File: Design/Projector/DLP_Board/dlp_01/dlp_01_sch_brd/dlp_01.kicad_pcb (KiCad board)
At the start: 6 copper layers, 22.3 x 6 mm, 255 parts, among them J1 Conn_02x40_Odd_Even, J10 Screw_Terminal_01x03, J2 Conn_02x40_Odd_Even, J3 Barrel_Jack_MountingPin, J4 Screw_Terminal_01x03, J5 Screw_Terminal_01x03, J6 Screw_Terminal_01x03, J7 Screw_Terminal_01x03, J8 Screw_Terminal_01x03, J9 Screw_Terminal_01x03, Q1 2N7000, U1 DLPC3437, U2 DLPC3437, U3 ASDMB-24.000MHZ-LC-T, U4 W25Q64JVSSIQ, U5 W25Q64JVSSIQ, U6 DLPA3000, U7 DLP3310AFQM, U8 RPM5.0-3.0, U9 NF_SN74AUP1T17

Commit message: Initial component placement on PCB
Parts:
- C1, C10, C11, C12, C13, C14, C15, C16, C17, C18, C19, C2, C20, C21, C22, C23, C24, C25, C26, C27, C28, C29, C3, C30, C31, C32, C33, C34, C35, C36, C37, C38, C39, C4, C40, C41, C42, C43, C44, C45, C46, C5, C6, C7, C8, C9: footprint Capacitors_SMD:C_0603 -> Capacitors_SMD:C_0402; moved to B.Cu
- C47, C48, C49, C50, C51, D5, J1, J10, J2, J3, J4, J5, Q1, R16, R52, R53, R54, R55, R92, R93, R94, R95, R96, R97, TP1, TP10, TP2, TP3, TP4, TP5, TP6, TP7, TP8, TP9, U3: moved to B.Cu
- FB1, FB2, FB3, FB4: value BLM18KG121TN1D -> BLM15PD800SN1D; footprint Inductors_SMD:L_0603 -> Inductors_SMD:L_0402; moved to B.Cu
- J6, J7, J8, J9: value Screw_Terminal_01x03 -> Conn_01x03_Male; footprint Connectors_Terminal_Blocks:TerminalBlock_bornier-3_P5.08mm -> Pin_Headers:Pin_Header_Straight_1x03_Pitch2.54mm_SMD_Pin1Left; moved to B.Cu
- moved C58 292.9 mm to (132.8, 139.9), turned to 180 degrees
- moved C52 292.0 mm to (130.0, 141.5), turned to 90 degrees
- moved R60 291.1 mm to (125.0, 144.5), turned to 180 degrees
- moved C55 289.4 mm to (127.8, 141.5), turned to 90 degrees
- moved D1 289.3 mm to (132.4, 137.9), turned to 180 degrees
- moved C68 288.4 mm to (125.0, 142.9), turned to 180 degrees
- moved R54 288.4 mm to (114.7, 142.3), turned to 270 degrees
- moved C48 287.8 mm to (116.7, 142.3), turned to 270 degrees
- moved C50 287.1 mm to (118.9, 142.3), turned to 270 degrees
- moved C74 285.8 mm to (125.8, 140.7), turned to 90 degrees
- moved C71 284.7 mm to (129.2, 131.9), turned to 180 degrees
- moved L3 284.0 mm to (132.6, 134.3), turned to 180 degrees
- moved L1 283.2 mm to (123.6, 140.7), turned to 270 degrees
- moved C66 281.6 mm to (121.0, 141.5), turned to 90 degrees
- moved C59 281.3 mm to (129.2, 129.7), turned to 180 degrees
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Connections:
- C12 pad 1: +1V1 -> +1V8
- C13 pad 1: +1V1 -> +1V8
- C15 pad 1: +1V1 -> +1V8
- C16 pad 1: +1V1 -> +1V8
- C18 pad 1: +1V1 -> +1V8
- C19 pad 1: +1V1 -> +1V8
- C21 pad 1: +1V1 -> +1V8
- C22 pad 1: +1V1 -> +1V8
- C24 pad 1: +1V1 -> +1V8
- C25 pad 1: +1V1 -> +1V8
- C26 pad 1: +1V1 -> +1V8
- C27 pad 1: +1V1 -> +1V8
- C29 pad 1: +1V1 -> +1V8
- C3 pad 1: +1V1 -> +1V8
- C30 pad 1: +1V1 -> +1V8
- C34 pad 1: +1V1 -> +1V8
- C35 pad 1: +1V1 -> +1V8
- C38 pad 1: +1V1 -> +1V8
- C39 pad 1: +1V1 -> +1V8
- C4 pad 1: +1V1 -> +1V8
- C41 pad 1: +1V1 -> +1V8
- C42 pad 1: +1V1 -> +1V8
- C8 pad 1: +1V1 -> +1V8
- C9 pad 1: +1V1 -> +1V8
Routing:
- net /dlp_controller/DMD_LS_RDATA: track 0.57 -> 23.3 mm
- net /dlp_controller/DMD_DEN_ARSTZ: track 0.57 -> 16.5 mm
- net /dlp_controller/sDMD_HS_WDATAG_P: track 0.57 -> 15.7 mm
- net /dlp_controller/sDMD_HS_CLK_P: track 0.57 -> 15.6 mm, vias 2 -> 3
- net /dlp_controller/sDMD_HS_WDATAG_N: track 0.57 -> 15.2 mm
- net /dlp_controller/mDMD_HS_WDATAD_N: track 0.57 -> 15.0 mm
- net /dlp_controller/mDMD_HS_WDATAD_P: track 0.57 -> 14.8 mm
- net /dlp_controller/sDMD_HS_WDATAA_N: track 0.57 -> 14.7 mm
- net /dlp_controller/mDMD_HS_WDATAC_N: track 0.57 -> 14.6 mm
- net /dlp_controller/sDMD_HS_WDATAE_N: track 0.57 -> 14.5 mm
- net /dlp_controller/mDMD_HS_WDATAH_N: track 0.57 -> 14.1 mm
- net /dlp_controller/sDMD_HS_WDATAF_N: track 0.57 -> 14.0 mm, vias 2 -> 3
- net /dlp_controller/mDMD_HS_CLK_N: track 0.57 -> 13.7 mm, vias 2 -> 3
- net /dlp_controller/mDMD_HS_WDATAC_P: track 0.57 -> 13.6 mm
- net /dlp_controller/mDMD_HS_WDATAB_N: track 0.59 -> 13.3 mm
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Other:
- board size 22.3 x 6 mm -> 102 x 98 mm
- net class Default: trace_width 0.1524 -> 0.1
- rule trace_min: 0.1524 -> 0.1

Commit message: Schematic and PCB complete ready for review
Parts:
- removed J10: Screw_Terminal_01x03, Connectors_Terminal_Blocks:TerminalBlock_bornier-3_P5.08mm
- removed R100, R101, R102, R103, R104, R105, R75, R76, R84, R85, R86, R87, R88, R90: 22R, Resistors_SMD:R_0603
- removed R79, R83: NF, Resistors_SMD:R_0603
- removed RN1, RN2, RN3: R_Pack08, Resistors_SMD:R_Array_Convex_8x0602
- removed RN4, RN5, RN6: 22R, Resistors_SMD:R_Array_Convex_8x0602
- added H1: 3mm, Mounting_Holes:MountingHole_3mm_Pad_Via, F.Cu at (99.6, 56.7)
- added H2: 3mm, Mounting_Holes:MountingHole_3mm_Pad_Via, F.Cu at (99.6, 147.0)
- added H3: 3mm, Mounting_Holes:MountingHole_3mm_Pad_Via, F.Cu at (195.5, 56.7)
- added H4: 3mm, Mounting_Holes:MountingHole_3mm_Pad_Via, F.Cu at (195.5, 147.0)
- added H5: 3mm, Mounting_Holes:MountingHole_3mm_Pad_Via, F.Cu at (99.6, 113.7)
- added H6: 3mm, Mounting_Holes:MountingHole_3mm_Pad_Via, F.Cu at (195.6, 113.6)
- C49, C51, C81, R55, R57, R97, TP2, TP3, TP4, TP5, TP6, TP7, TP8, TP9: moved to F.Cu
- C53, C56, C57, C61, C66, R10, R11, R12, R19, R35, R36, R37, R39, R41, R42, R43, R44, R46, R47, R51, R81, R82: moved to B.Cu
- R72, R73, R74: value 22R -> NF
- moved TP8 58.2 mm to (157.5, 93.6)
- moved TP9 56.4 mm to (155.2, 93.6)
- moved TP7 53.1 mm to (157.5, 95.9)
- moved TP6 51.1 mm to (155.2, 95.9)
- moved TP5 49.7 mm to (155.2, 98.2)
- moved TP3 48.8 mm to (157.5, 98.2)
- moved TP4 48.4 mm to (155.2, 100.5)
- moved TP2 46.7 mm to (157.5, 100.5)
- moved R81 45.7 mm to (132.5, 117.4), turned to 90 degrees
- moved R82 42.4 mm to (134.1, 117.4), turned to 270 degrees
- moved R29 34.0 mm to (133.6, 105.2), turned to 90 degrees
- moved R89 33.5 mm to (121.2, 109.8), turned to 180 degrees
- moved R71 32.7 mm to (124.8, 66.5), turned to 270 degrees
- moved R12 31.1 mm to (133.4, 121.4), turned to 0 degrees
- moved R28 31.0 mm to (135.2, 105.2), turned to 270 degrees
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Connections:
- net /application_connectors/3DR_A renamed Net-(R50-Pad1)
- net /application_connectors/3DR_B renamed Net-(R48-Pad1)
- J1 pad 15: Net-(J1-Pad15) -> /application_connectors/ZYNQ_VDDIO_13
- J1 pad 19: /application_connectors/IO_B13_LN13 -> /application_connectors/PDM_CVS_TE_B
- J1 pad 21: /application_connectors/IO_B13_LP15 -> /application_connectors/HSYNC_B
- J1 pad 23: /application_connectors/IO_B13_LN15 -> /application_connectors/VSYNC_B
- J1 pad 27: /application_connectors/IO_B34_LP2 -> /application_connectors/DATEN_B
- J1 pad 49: Net-(J1-Pad49) -> /application_connectors/ZYNQ_VDDIO_34
- J2 pad 33: /application_connectors/IO_B35_LP5 -> /application_connectors/FPGA_RDY
- J2 pad 35: /application_connectors/IO_B35_LN5 -> /application_connectors/ACT_SYNC
- J2 pad 37: /application_connectors/IO_B35_LP7 -> /application_connectors/SUB_FRAME
- J2 pad 39: /application_connectors/IO_B35_LN7 -> /application_connectors/PROJ_ON
- J2 pad 43: /application_connectors/IO_B35_LP9 -> /application_connectors/sHOST_IRQ
- J2 pad 45: /application_connectors/IO_B35_LN9 -> /application_connectors/mHOST_IRQ
- J2 pad 46: /application_connectors/IO_B35_LP12 -> /application_connectors/PCLK_A
- J2 pad 51: Net-(J2-Pad51) -> /application_connectors/ZYNQ_VDDIO_35
- J2 pad 53: /application_connectors/IO_B35_LP13 -> /application_connectors/PCLK_B
- J2 pad 65: /application_connectors/IO_B35_LN17 -> /application_connectors/PDM_CVS_TE_A
- J2 pad 67: /application_connectors/IO_B35_LP19 -> /application_connectors/HSYNC_A
- J2 pad 69: /application_connectors/IO_B35_LN19 -> /application_connectors/VSYNC_A
- J2 pad 73: /application_connectors/IO_B35_LP21 -> /application_connectors/DATEN_A
- J3 pad 3: Net-(J3-Pad3) -> GND
- R68 pad 1: Net-(J1-Pad49) -> /application_connectors/ZYNQ_VDDIO_34
- R68 pad 2: /application_connectors/ZYNQ_VDDIO_34 -> +3V3
- R69 pad 1: Net-(J1-Pad15) -> /application_connectors/ZYNQ_VDDIO_13
- R69 pad 2: /application_connectors/ZYNQ_VDDIO_13 -> +3V3
- R72 pad 1: /application_connectors/IO_B13_LN13 -> /application_connectors/ZYNQ_VDDIO_34
- R72 pad 2: /application_connectors/PDM_CVS_TE_B -> +1V8
- R73 pad 1: /application_connectors/IO_B13_LP15 -> /application_connectors/ZYNQ_VDDIO_13
- R73 pad 2: /application_connectors/HSYNC_B -> +1V8
- R74 pad 1: /application_connectors/IO_B13_LN15 -> /application_connectors/ZYNQ_VDDIO_35
- R74 pad 2: /application_connectors/VSYNC_B -> +1V8
- R78 pad 1: Net-(J2-Pad51) -> /application_connectors/ZYNQ_VDDIO_35
- R78 pad 2: /application_connectors/ZYNQ_VDDIO_35 -> +3V3
- U1 pad K1: /application_connectors/PDAT_B_1 -> /application_connectors/LCD_DATA1
- U1 pad K2: /application_connectors/PDAT_B_0 -> /application_connectors/LCD_DATA0
- U1 pad L1: /application_connectors/PDAT_B_3 -> /application_connectors/LCD_DATA3
- U1 pad L2: /application_connectors/PDAT_B_2 -> /application_connectors/LCD_DATA2
- U1 pad M1: /application_connectors/PDAT_B_5 -> /application_connectors/LCD_DATA5
- U1 pad M2: /application_connectors/PDAT_B_4 -> /application_connectors/LCD_DATA4
- U1 pad N1: /application_connectors/PDAT_B_7 -> /application_connectors/LCD_DATA7
- U1 pad N2: /application_connectors/PDAT_B_6 -> /application_connectors/LCD_DATA6
- U1 pad P10: /application_connectors/PDAT_B_23 -> /application_connectors/IO_B34_LP4
- U1 pad P4: /application_connectors/PDAT_B_11 -> /application_connectors/LCD_DATA11
- U1 pad P5: /application_connectors/PDAT_B_13 -> /application_connectors/LCD_DATA13
- U1 pad P6: /application_connectors/PDAT_B_15 -> /application_connectors/LCD_DATA15
- U1 pad P7: /application_connectors/PDAT_B_17 -> /application_connectors/IO_B34_LP11
- U1 pad P8: /application_connectors/PDAT_B_19 -> /application_connectors/IO_B34_LP8
- U1 pad P9: /application_connectors/PDAT_B_21 -> /application_connectors/IO_B34_LP6
- U1 pad R1: /application_connectors/PDAT_B_8 -> /application_connectors/LCD_DATA8
- U1 pad R2: /application_connectors/PDAT_B_9 -> /application_connectors/LCD_DATA9
- U1 pad R3: /application_connectors/PDAT_B_10 -> /application_connectors/LCD_DATA10
- U1 pad R4: /application_connectors/PDAT_B_12 -> /application_connectors/LCD_DATA12
- U1 pad R5: /application_connectors/PDAT_B_14 -> /application_connectors/LCD_DATA14
- U1 pad R6: /application_connectors/PDAT_B_16 -> /application_connectors/IO_B34_LN11
- U1 pad R7: /application_connectors/PDAT_B_18 -> /application_connectors/IO_B34_LN8
- U1 pad R8: /application_connectors/PDAT_B_20 -> /application_connectors/IO_B34_LN6
- U1 pad R9: /application_connectors/PDAT_B_22 -> /application_connectors/IO_B34_LN4
- U2 pad K1: /dlp_controller/dlp_controller_datainterface/PDAT_A_1 -> /application_connectors/IO_B35_LN23
- U2 pad K2: /dlp_controller/dlp_controller_datainterface/PDAT_A_0 -> /application_connectors/IO_B35_LP23
- U2 pad L1: /application_connectors/PDAT_A_3 -> /application_connectors/IO_B35_LP24
- U2 pad L2: /application_connectors/PDAT_A_2 -> /application_connectors/IO_B35_LN24
- U2 pad M1: /application_connectors/PDAT_A_5 -> /application_connectors/IO_B35_LP22
- U2 pad M2: /application_connectors/PDAT_A_4 -> /application_connectors/IO_B35_LN22
- U2 pad N1: /application_connectors/PDAT_A_7 -> /application_connectors/IO_B35_LP20
- U2 pad N2: /application_connectors/PDAT_A_6 -> /application_connectors/IO_B35_LN20
- U2 pad P10: /application_connectors/PDAT_A_23 -> /application_connectors/IO_B35_LP2
- U2 pad P4: /application_connectors/PDAT_A_11 -> /application_connectors/IO_B35_LP16
- U2 pad P5: /application_connectors/PDAT_A_13 -> /application_connectors/IO_B35_LP14
- U2 pad P6: /application_connectors/PDAT_A_15 -> /application_connectors/IO_B35_LP10
- U2 pad P7: /application_connectors/PDAT_A_17 -> /application_connectors/IO_B35_LP8
- U2 pad P8: /application_connectors/PDAT_A_19 -> /application_connectors/IO_B35_LP6
- U2 pad P9: /application_connectors/PDAT_A_21 -> /application_connectors/IO_B35_LP4
- U2 pad R1: /application_connectors/PDAT_A_8 -> /application_connectors/IO_B35_LN18
- U2 pad R2: /application_connectors/PDAT_A_9 -> /application_connectors/IO_B35_LP18
- U2 pad R3: /application_connectors/PDAT_A_10 -> /application_connectors/IO_B35_LN16
- U2 pad R4: /application_connectors/PDAT_A_12 -> /application_connectors/IO_B35_LN14
- U2 pad R5: /application_connectors/PDAT_A_14 -> /application_connectors/IO_B35_LN10
- U2 pad R6: /application_connectors/PDAT_A_16 -> /application_connectors/IO_B35_LN8
- U2 pad R7: /application_connectors/PDAT_A_18 -> /application_connectors/IO_B35_LN6
- U2 pad R8: /application_connectors/PDAT_A_20 -> /application_connectors/IO_B35_LN4
- U2 pad R9: /application_connectors/PDAT_A_22 -> /application_connectors/IO_B35_LN2
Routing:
- net +3V3: track 0.00 -> 271.0 mm, vias 0 -> 16
- net GND: track 55.4 -> 323.2 mm, vias 119 -> 242
- net +1V8: track 13.7 -> 235.1 mm, vias 39 -> 64
- net /dlp_pmic/LED_ANODE: track 0.00 -> 133.0 mm, vias 0 -> 2
- net /dlp_pmic/LEDx_CATHODE: track 0.00 -> 128.5 mm, vias 0 -> 2
- net /application_connectors/PDM_CVS_TE_B: track 0.57 -> 125.6 mm, vias 1 -> 7
- net /dlp_controller/SPI1_CLK: track 0.00 -> 106.0 mm, vias 0 -> 4
- net /application_connectors/HSYNC_B: track 0.57 -> 105.0 mm, vias 1 -> 4
- net /dlp_controller/SPI1_DOUT: track 0.00 -> 102.5 mm, vias 0 -> 4
- net /SENS_FOCUS: track 0.00 -> 98.0 mm, vias 0 -> 4
- net /application_connectors/VSYNC_B: track 0.57 -> 98.4 mm, vias 1 -> 4
- net /SENS_LABB: track 0.00 -> 97.0 mm, vias 0 -> 4
- net /dlp_controller/SPI1_CSZ0: track 0.00 -> 96.0 mm, vias 0 -> 4
- net /application_connectors/DATEN_B: track 0.57 -> 94.1 mm, vias 1 -> 4
- net /application_connectors/LCD_DATA0: track 0.00 -> 91.1 mm, vias 0 -> 4
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- added copper zone on B.Cu, net +12V
- added copper zone on F.Cu, net +12V
- added copper zone on In2.Cu, net +1V1
- added copper zone on B.Cu, net +1V8
- added copper zone on In2.Cu, net +1V8
- added copper zone on B.Cu, net /application_connectors/ZYNQ_VDDIO_13
- added copper zone on F.Cu, net /application_connectors/ZYNQ_VDDIO_13
- added copper zone on B.Cu, net /application_connectors/ZYNQ_VDDIO_34
- added copper zone on F.Cu, net /application_connectors/ZYNQ_VDDIO_34
- added copper zone on B.Cu, net /application_connectors/ZYNQ_VDDIO_35
- added copper zone on F.Cu, net /application_connectors/ZYNQ_VDDIO_35
- added copper zone on F.Cu, net GND
- added copper zone on In1.Cu, net GND
- added copper zone on B.Cu, net Net-(C48-Pad2)
- added copper zone on F.Cu, net Net-(C48-Pad2)
- added copper zone on F.Cu, net Net-(C93-Pad1)
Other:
- net class Default: trace_width 0.1 -> 0.15
- rule trace_min: 0.1 -> 0.09

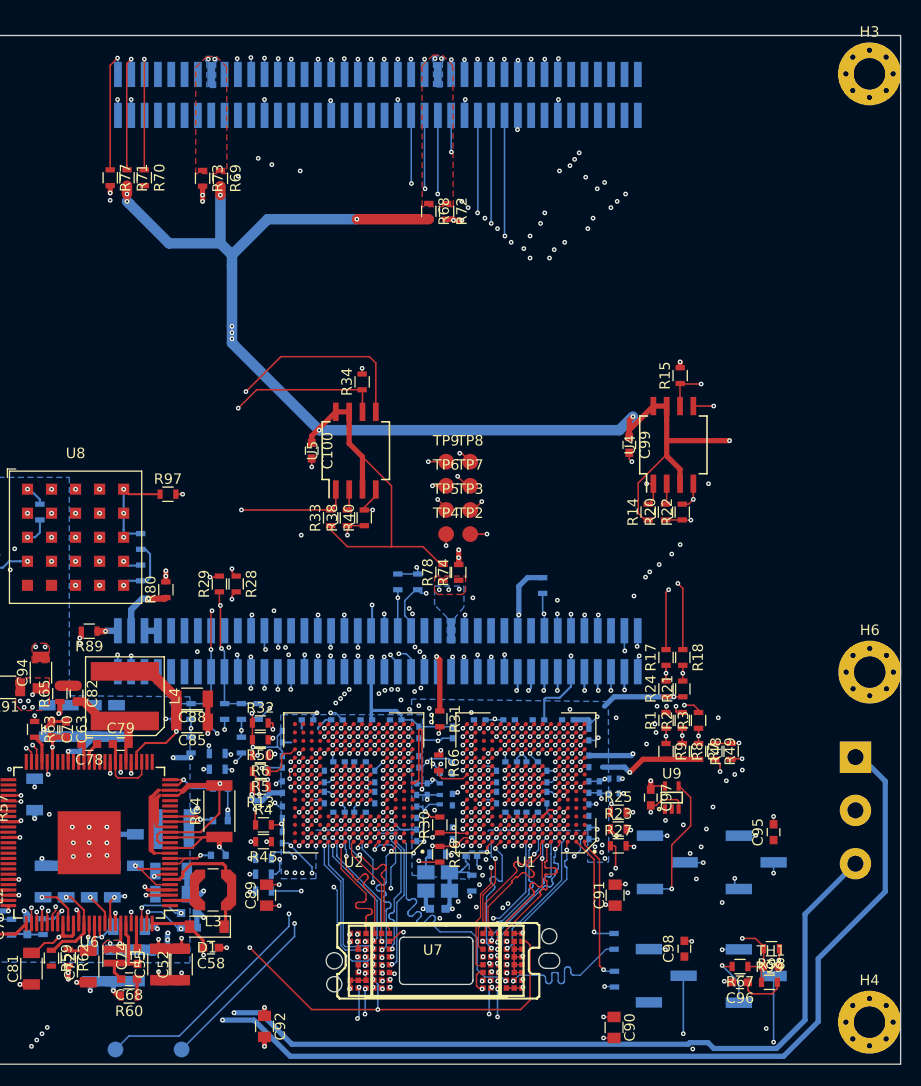
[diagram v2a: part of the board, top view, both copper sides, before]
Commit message: Final PCB tweaks and 3D model export
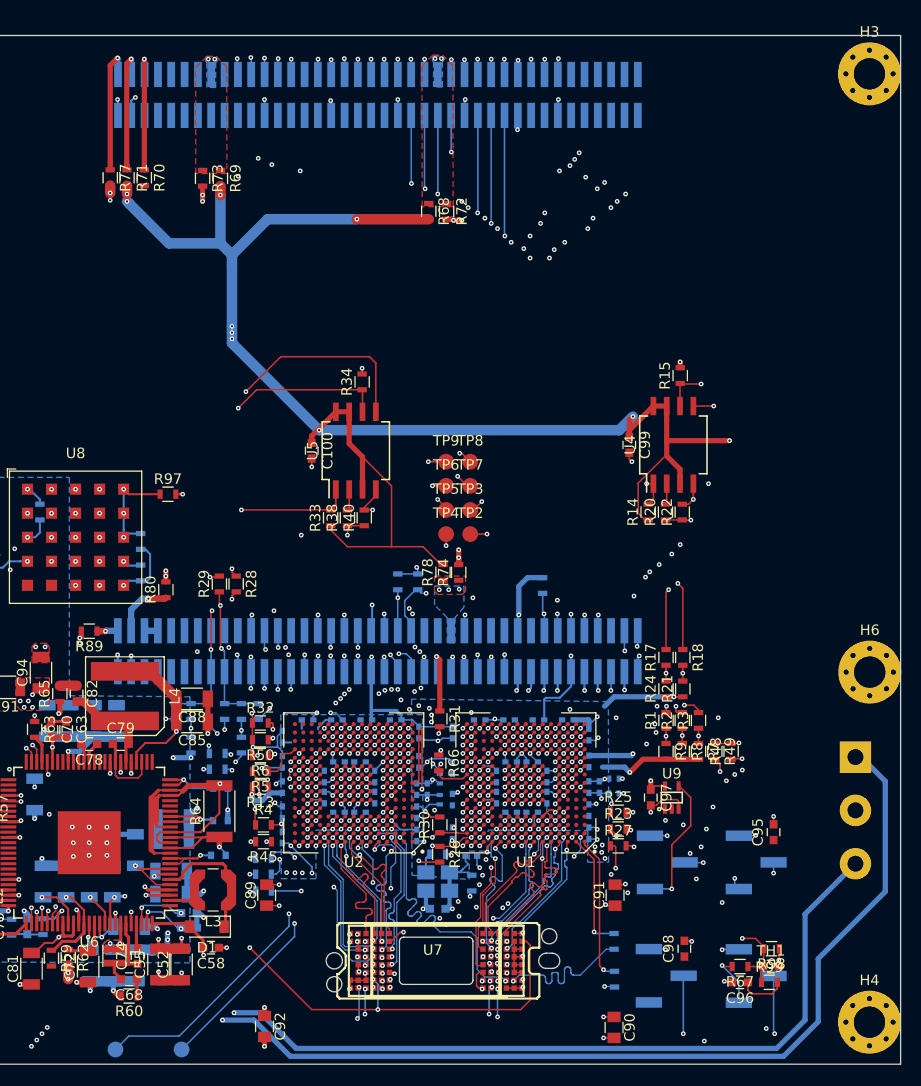
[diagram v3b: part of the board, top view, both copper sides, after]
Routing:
- net +3V3: track 271.0 -> 273.6 mm
- net +5V: track 90.1 -> 91.4 mm
